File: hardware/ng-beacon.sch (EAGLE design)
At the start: 7 parts

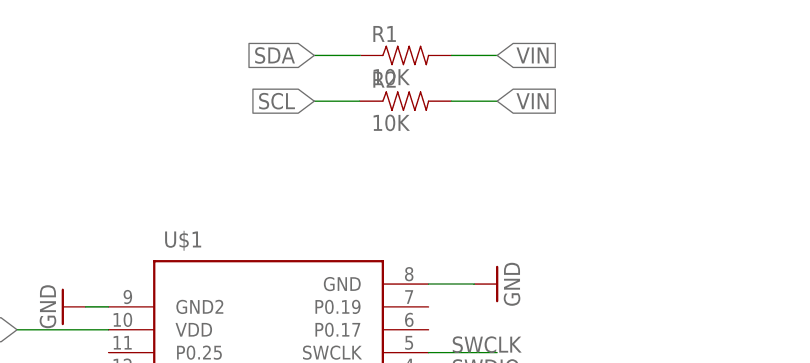
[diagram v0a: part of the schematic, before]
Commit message: fix(pcb): remove I2C pullup resistors
it works fine without them, as the nRF51 has internal pullups
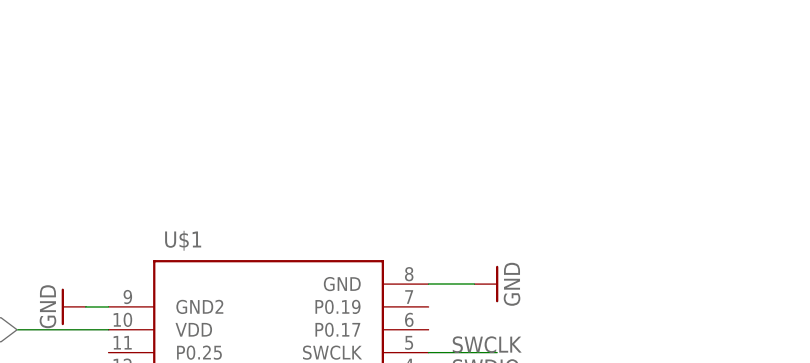
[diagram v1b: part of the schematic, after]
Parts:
- removed R1, R2: 10K, SparkFun-Resistors:10KOHM-1/10W-1%(0603)0603
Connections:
- net SCL: no longer R2.1
- net SDA: no longer R1.1
- net VIN: no longer R1.2, R2.2
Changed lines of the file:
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@@
 <part name="SN1" library="sensirion" deviceset="SHT21" device=""/>
 <part name="GND4" library="SparkFun-Aesthetics" deviceset="GND" device=""/>
-<part name="R1" library="SparkFun-Resistors" deviceset="10KOHM-1/10W-1%(0603)" device="0603" value="10K"/>
-<part name="R2" library="SparkFun-Resistors" deviceset="10KOHM-1/10W-1%(0603)" device="0603" value="10K"/>
 </parts>
 <sheets>
@@
 <instance part="SN1" gate="G$1" x="106.68" y="38.1"/>
 <instance part="GND4" gate="1" x="83.82" y="30.48" rot="R270"/>
-<instance part="R1" gate="G$1" x="45.72" y="93.98"/>
-<instance part="R2" gate="G$1" x="45.72" y="88.9"/>
 </instances>
 <busses>
@@
 <label x="86.36" y="45.72" size="1.778" layer="95"/>
 </segment>
-<segment>
-<pinref part="R1" gate="G$1" pin="2"/>
-<wire x1="50.8" y1="93.98" x2="55.88" y2="93.98" width="0.1524" layer="91"/>
-<label x="55.88" y="93.98" size="1.778" layer="95" xref="yes"/>
-</segment>
-<segment>
-<pinref part="R2" gate="G$1" pin="2"/>
-<wire x1="50.8" y1="88.9" x2="55.88" y2="88.9" width="0.1524" layer="91"/>
-<label x="55.88" y="88.9" size="1.778" layer="95" xref="yes"/>
-</segment>
 </net>
 <net name="SWCLK" class="0">
@@
 <label x="86.36" y="40.64" size="1.778" layer="95"/>
 </segment>
-<segment>
-<pinref part="R1" gate="G$1" pin="1"/>
-<wire x1="35.56" y1="93.98" x2="40.64" y2="93.98" width="0.1524" layer="91"/>
-<label x="35.56" y="93.98" size="1.778" layer="95" rot="R180" xref="yes"/>
-</segment>
 </net>
 <net name="SCL" class="0">
@@
 <label x="86.36" y="35.56" size="1.778" layer="95"/>
 </segment>
-<segment>
-<pinref part="R2" gate="G$1" pin="1"/>
-<wire x1="40.64" y1="88.9" x2="35.56" y2="88.9" width="0.1524" layer="91"/>
-<label x="35.56" y="88.9" size="1.778" layer="95" rot="R180" xref="yes"/>
-</segment>
 </net>

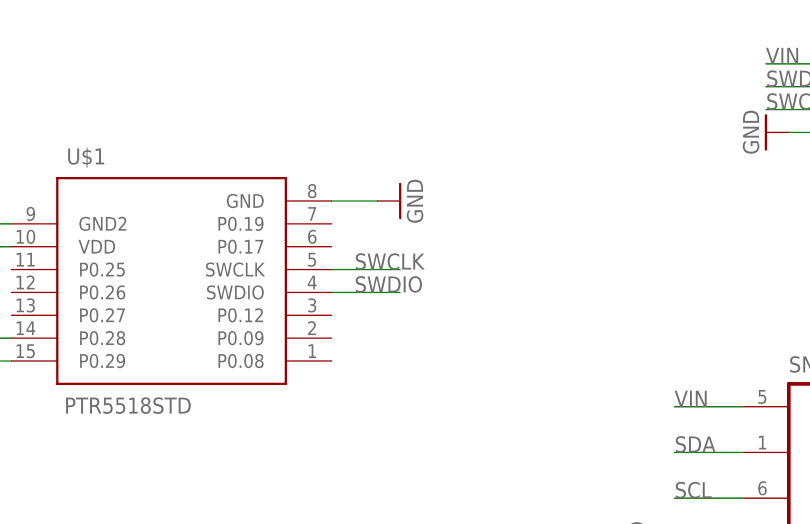
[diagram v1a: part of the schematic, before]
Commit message: feat: add DFU pads
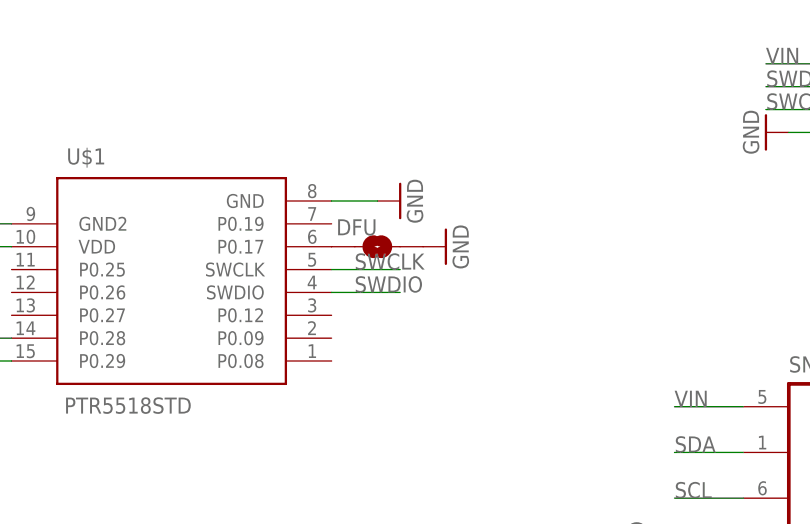
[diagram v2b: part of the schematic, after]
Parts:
- added DFU: JUMPER-PAD-2-NO, SparkFun-Passives:JUMPER-PAD-2-NO
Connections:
- new net N$4: DFU.1, U$1.P0.17
- net GND: now also DFU.2
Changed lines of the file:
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@@
 <part name="SN1" library="sensirion" deviceset="SHT21" device=""/>
 <part name="GND4" library="SparkFun-Aesthetics" deviceset="GND" device=""/>
+<part name="DFU" library="SparkFun-Passives" deviceset="JUMPER-PAD-2-NO" device=""/>
+<part name="GND5" library="SparkFun-Aesthetics" deviceset="GND" device=""/>
 </parts>
 <sheets>
@@
 <instance part="SN1" gate="G$1" x="106.68" y="38.1"/>
 <instance part="GND4" gate="1" x="83.82" y="30.48" rot="R270"/>
+<instance part="DFU" gate="G$1" x="53.34" y="63.5" smashed="yes">
+<attribute name="NAME" x="48.768" y="64.77" size="1.778" layer="95"/>
+</instance>
+<instance part="GND5" gate="1" x="60.96" y="63.5" rot="R90"/>
 </instances>
 <busses>
@@
 <wire x1="93.98" y1="30.48" x2="86.36" y2="30.48" width="0.1524" layer="91"/>
 <pinref part="GND4" gate="1" pin="GND"/>
+</segment>
+<segment>
+<pinref part="DFU" gate="G$1" pin="2"/>
+<pinref part="GND5" gate="1" pin="GND"/>
 </segment>
 </net>
@@
 </segment>
 </net>
+<net name="N$4" class="0">
+<segment>
+<pinref part="U$1" gate="G$1" pin="P0.17"/>
+<pinref part="DFU" gate="G$1" pin="1"/>
+</segment>
+</net>

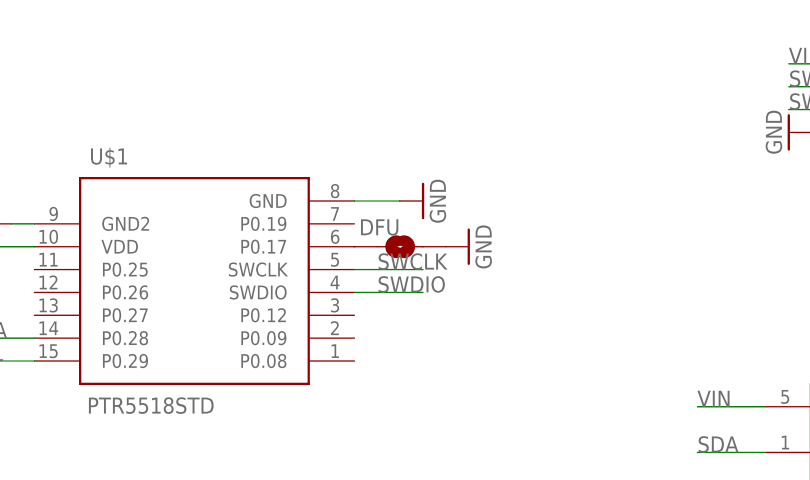
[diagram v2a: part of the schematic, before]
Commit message: fix: update board layout for PTR5618
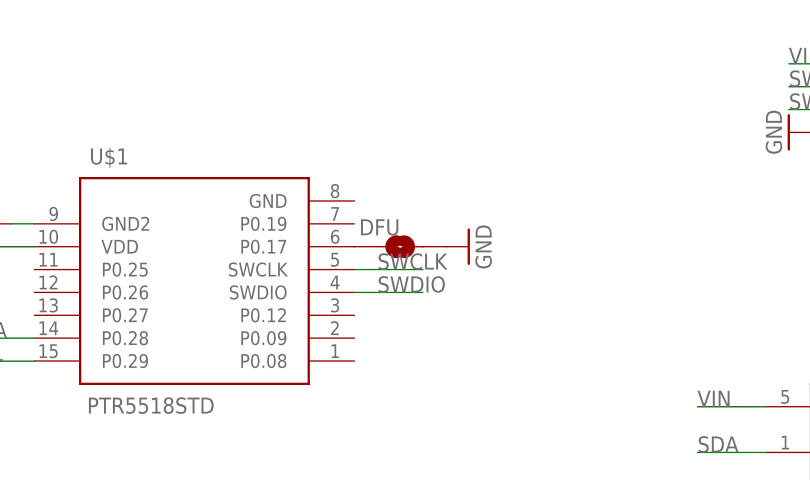
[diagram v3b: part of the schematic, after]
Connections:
- net GND: no longer U$1.GND
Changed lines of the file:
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@@
 <part name="S1" library="SparkFun-Electromechanical" deviceset="SWITCH-DPDT" device="AYZ0202" value="DPDT"/>
 <part name="GND1" library="SparkFun-Aesthetics" deviceset="GND" device=""/>
-<part name="GND2" library="SparkFun-Aesthetics" deviceset="GND" device=""/>
 <part name="GND3" library="SparkFun-Aesthetics" deviceset="GND" device=""/>
 <part name="J1" library="SparkFun-Connectors" deviceset="M04" device="LOCK"/>
@@
 <instance part="S1" gate="G$1" x="-20.32" y="48.26" rot="R180"/>
 <instance part="GND1" gate="1" x="-17.78" y="76.2" rot="R90"/>
-<instance part="GND2" gate="1" x="55.88" y="68.58" rot="R90"/>
 <instance part="GND3" gate="1" x="7.62" y="66.04" rot="R270"/>
 <instance part="J1" gate="G$1" x="111.76" y="81.28" rot="R180"/>
@@
 </segment>
 <segment>
-<pinref part="U$1" gate="G$1" pin="GND"/>
-<wire x1="53.34" y1="68.58" x2="48.26" y2="68.58" width="0.1524" layer="91"/>
-<pinref part="GND2" gate="1" pin="GND"/>
-</segment>
-<segment>

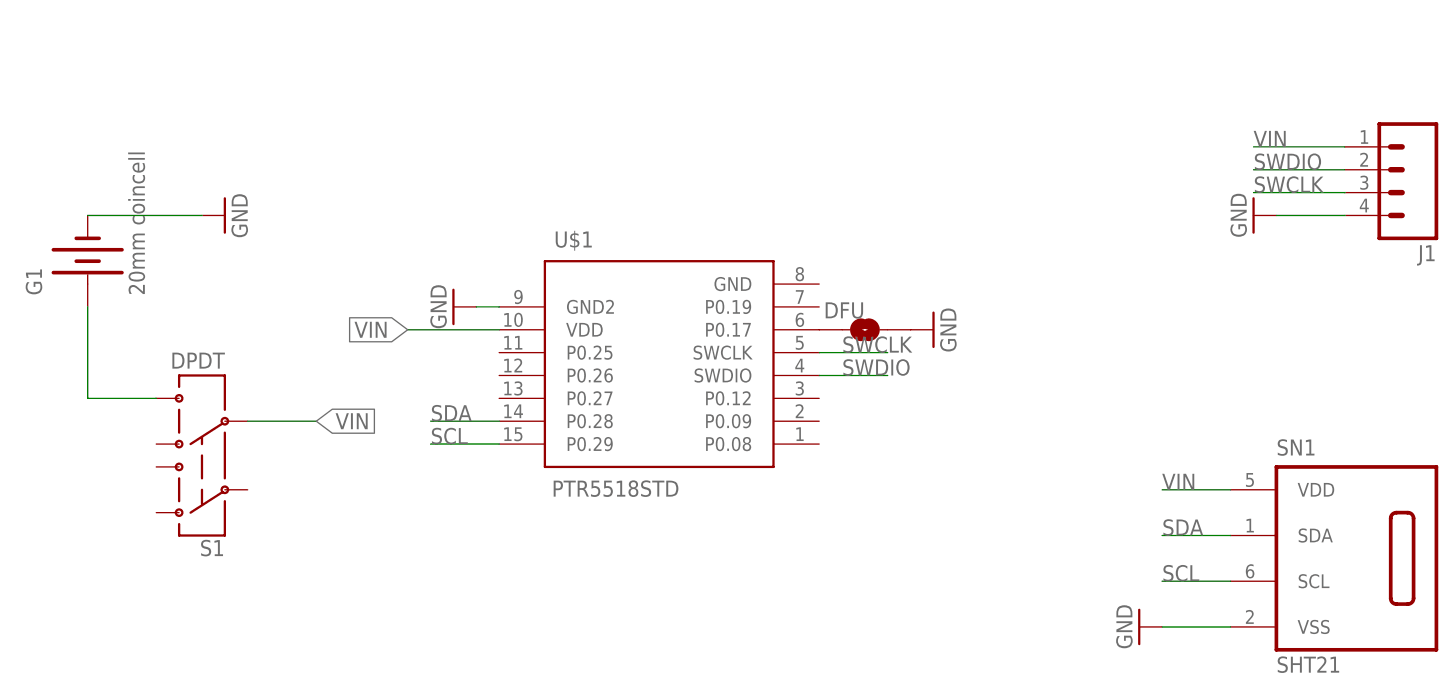
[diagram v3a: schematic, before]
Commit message: Add a prototype area with PO.26, 27, SDA, and SCL.
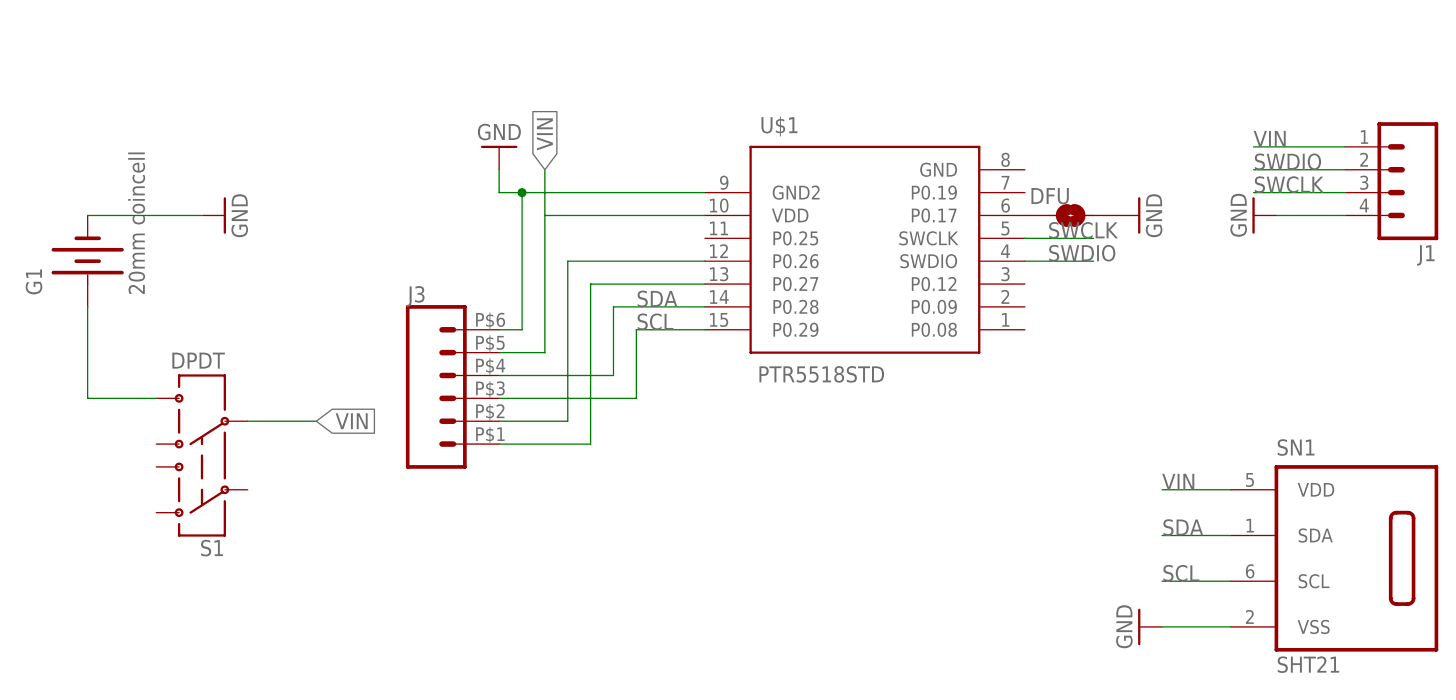
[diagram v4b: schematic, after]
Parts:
- added J3: (no value), heathkit:CONN_06
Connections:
- new net N$5: J3.2, U$1.P0.26
- new net N$6: J3.1, U$1.P0.27
- net GND: now also J3.6
- net SCL: now also J3.3
- net SDA: now also J3.4
- net VIN: now also J3.5
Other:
- moved on the sheet: DFU, U$1
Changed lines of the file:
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@@
 <?xml version="1.0" encoding="utf-8"?>
 <!DOCTYPE eagle SYSTEM "eagle.dtd">
-<eagle version="7.6.0">
+<eagle version="8.0.2">
 <drawing>
 <settings>
@@
 <part name="DFU" library="SparkFun-Passives" deviceset="JUMPER-PAD-2-NO" device=""/>
 <part name="GND5" library="SparkFun-Aesthetics" deviceset="GND" device=""/>
+<part name="J3" library="heathkit" deviceset="CONN_06" device=""/>
 </parts>
 <sheets>
@@
 </plain>
 <instances>
-<instance part="U$1" gate="G$1" x="30.48" y="58.42"/>
+<instance part="U$1" gate="G$1" x="53.34" y="71.12"/>
 <instance part="G1" gate="G$1" x="-33.02" y="71.12" rot="R90"/>
 <instance part="S1" gate="G$1" x="-20.32" y="48.26" rot="R180"/>
 <instance part="GND1" gate="1" x="-17.78" y="76.2" rot="R90"/>
-<instance part="GND3" gate="1" x="7.62" y="66.04" rot="R270"/>
+<instance part="GND3" gate="1" x="12.7" y="83.82" rot="R180"/>
 <instance part="J1" gate="G$1" x="111.76" y="81.28" rot="R180"/>
 <instance part="GND8" gate="1" x="96.52" y="76.2" rot="R270"/>
 <instance part="SN1" gate="G$1" x="106.68" y="38.1"/>
 <instance part="GND4" gate="1" x="83.82" y="30.48" rot="R270"/>
-<instance part="DFU" gate="G$1" x="53.34" y="63.5" smashed="yes">
-<attribute name="NAME" x="48.768" y="64.77" size="1.778" layer="95"/>
+<instance part="DFU" gate="G$1" x="76.2" y="76.2" smashed="yes">
+<attribute name="NAME" x="71.628" y="77.47" size="1.778" layer="95"/>
 </instance>
-<instance part="GND5" gate="1" x="60.96" y="63.5" rot="R90"/>
+<instance part="GND5" gate="1" x="83.82" y="76.2" rot="R90"/>
+<instance part="J3" gate="G$1" x="7.62" y="55.88"/>
 </instances>
 <busses>
@@
 <segment>
 <pinref part="U$1" gate="G$1" pin="GND2"/>
-<wire x1="10.16" y1="66.04" x2="12.7" y2="66.04" width="0.1524" layer="91"/>
+<wire x1="12.7" y1="81.28" x2="12.7" y2="78.74" width="0.1524" layer="91"/>
+<wire x1="12.7" y1="78.74" x2="15.24" y2="78.74" width="0.1524" layer="91"/>
 <pinref part="GND3" gate="1" pin="GND"/>
+<pinref part="J3" gate="G$1" pin="6"/>
+<wire x1="15.24" y1="78.74" x2="35.56" y2="78.74" width="0.1524" layer="91"/>
+<wire x1="12.7" y1="63.5" x2="15.24" y2="63.5" width="0.1524" layer="91"/>
+<wire x1="15.24" y1="63.5" x2="15.24" y2="78.74" width="0.1524" layer="91"/>
+<junction x="15.24" y="78.74"/>
 </segment>
 <segment>
@@
 <segment>
 <pinref part="U$1" gate="G$1" pin="VDD"/>
-<wire x1="12.7" y1="63.5" x2="2.54" y2="63.5" width="0.1524" layer="91"/>
-<label x="2.54" y="63.5" size="1.778" layer="95" rot="R180" xref="yes"/>
+<wire x1="35.56" y1="76.2" x2="17.78" y2="76.2" width="0.1524" layer="91"/>
+<wire x1="17.78" y1="76.2" x2="17.78" y2="81.28" width="0.1524" layer="91"/>
+<label x="17.78" y="81.28" size="1.778" layer="95" rot="R90" xref="yes"/>
+<wire x1="17.78" y1="76.2" x2="17.78" y2="60.96" width="0.1524" layer="91"/>
+<pinref part="J3" gate="G$1" pin="5"/>
+<wire x1="12.7" y1="60.96" x2="17.78" y2="60.96" width="0.1524" layer="91"/>
 </segment>
 <segment>
@@
 <segment>
 <pinref part="U$1" gate="G$1" pin="SWCLK"/>
-<wire x1="48.26" y1="60.96" x2="55.88" y2="60.96" width="0.1524" layer="91"/>
-<label x="50.8" y="60.96" size="1.778" layer="95"/>
+<wire x1="71.12" y1="73.66" x2="78.74" y2="73.66" width="0.1524" layer="91"/>
+<label x="73.66" y="73.66" size="1.778" layer="95"/>
 </segment>
 </net>
@@
 <segment>
 <pinref part="U$1" gate="G$1" pin="SWDIO"/>
-<wire x1="48.26" y1="58.42" x2="55.88" y2="58.42" width="0.1524" layer="91"/>
-<label x="50.8" y="58.42" size="1.778" layer="95"/>
+<wire x1="71.12" y1="71.12" x2="78.74" y2="71.12" width="0.1524" layer="91"/>
+<label x="73.66" y="71.12" size="1.778" layer="95"/>
 </segment>
 </net>
@@
 <segment>
 <pinref part="U$1" gate="G$1" pin="P0.28"/>
-<wire x1="12.7" y1="53.34" x2="5.08" y2="53.34" width="0.1524" layer="91"/>
-<label x="5.08" y="53.34" size="1.778" layer="95"/>
+<label x="27.94" y="66.04" size="1.778" layer="95"/>
+<wire x1="35.56" y1="66.04" x2="25.4" y2="66.04" width="0.1524" layer="91"/>
+<pinref part="J3" gate="G$1" pin="4"/>
+<wire x1="12.7" y1="58.42" x2="25.4" y2="58.42" width="0.1524" layer="91"/>
+<wire x1="25.4" y1="58.42" x2="25.4" y2="66.04" width="0.1524" layer="91"/>
 </segment>
 <segment>
@@
 <segment>
 <pinref part="U$1" gate="G$1" pin="P0.29"/>
-<wire x1="12.7" y1="50.8" x2="5.08" y2="50.8" width="0.1524" layer="91"/>
-<label x="5.08" y="50.8" size="1.778" layer="95"/>
+<label x="27.94" y="63.5" size="1.778" layer="95"/>
+<wire x1="35.56" y1="63.5" x2="27.94" y2="63.5" width="0.1524" layer="91"/>
+<pinref part="J3" gate="G$1" pin="3"/>
+<wire x1="12.7" y1="55.88" x2="27.94" y2="55.88" width="0.1524" layer="91"/>
+<wire x1="27.94" y1="55.88" x2="27.94" y2="63.5" width="0.1524" layer="91"/>
 </segment>
 <segment>
@@
 </segment>
 </net>
+<net name="N$5" class="0">
+<segment>
+<wire x1="20.32" y1="53.34" x2="20.32" y2="71.12" width="0.1524" layer="91"/>
+<pinref part="U$1" gate="G$1" pin="P0.26"/>
+<wire x1="20.32" y1="71.12" x2="35.56" y2="71.12" width="0.1524" layer="91"/>
+<pinref part="J3" gate="G$1" pin="2"/>
+<wire x1="12.7" y1="53.34" x2="20.32" y2="53.34" width="0.1524" layer="91"/>
+</segment>
+</net>
+<net name="N$6" class="0">
+<segment>
+<wire x1="22.86" y1="50.8" x2="22.86" y2="68.58" width="0.1524" layer="91"/>
+<pinref part="U$1" gate="G$1" pin="P0.27"/>
+<wire x1="22.86" y1="68.58" x2="35.56" y2="68.58" width="0.1524" layer="91"/>
+<pinref part="J3" gate="G$1" pin="1"/>
+<wire x1="12.7" y1="50.8" x2="22.86" y2="50.8" width="0.1524" layer="91"/>
+</segment>
+</net>
